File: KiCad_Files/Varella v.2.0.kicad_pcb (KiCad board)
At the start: 4 copper layers, 86 x 86 mm, 97 parts, among them IC1 MAX6682MUA+T, IC2 MAX6682MUA+T, IC3 MAX6682MUA+T, IC4 MMC5983MA, IC5 ZMOD4410AI3V, J1 ESQ-120-39-G-D, J2 Conn_01x12_Male, J3 MEM2075-00-140-01-A, J4 53261-7002, J5 53261-7002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

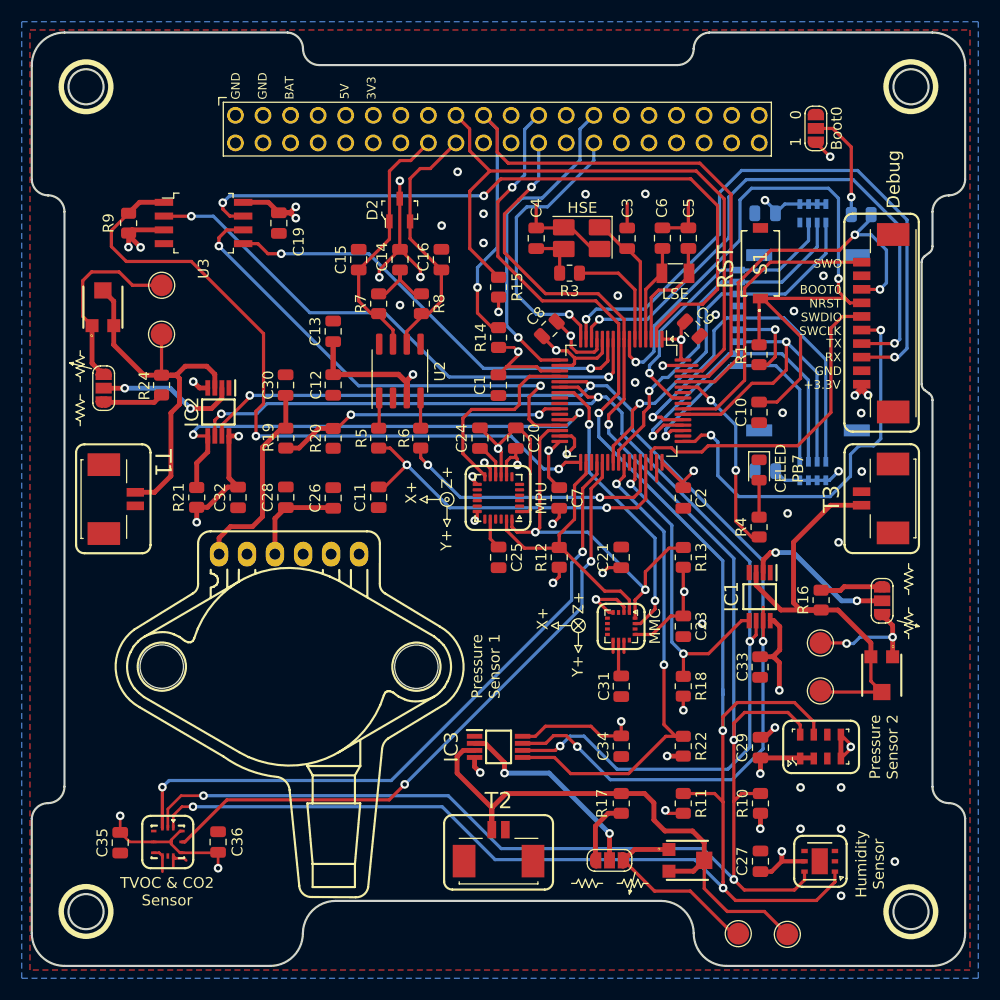
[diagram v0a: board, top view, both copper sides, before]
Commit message: Add Traces to Stack Connector
Connects the Interrupts and PWM pins that come from the EPS boards through the Stack Connector to Varella's STM32.
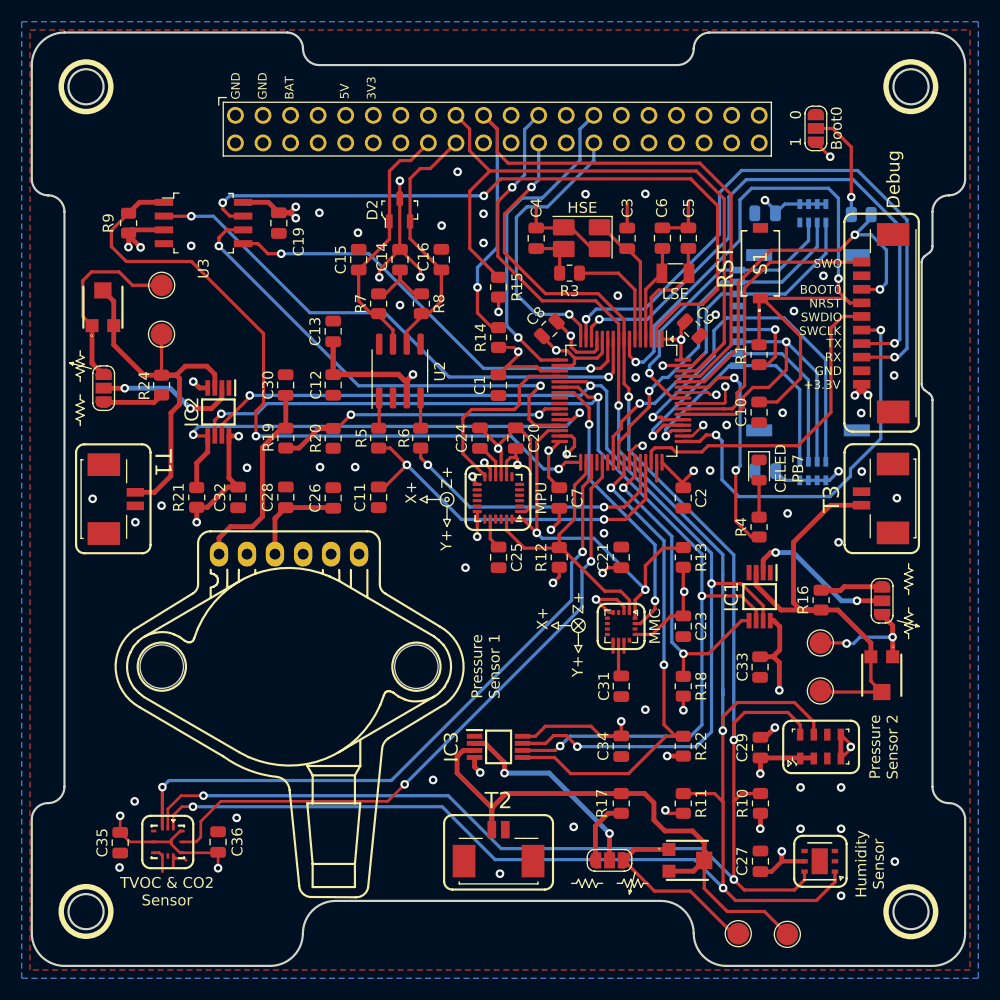
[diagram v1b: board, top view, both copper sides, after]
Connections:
- J1 pad 33: Net-(J1-Pad33) -> EPS_ALRT1
- J1 pad 34: Net-(J1-Pad34) -> EPS_CHRG
- J1 pad 35: Net-(J1-Pad35) -> EPS_THERM_PWM
- J1 pad 37: Net-(J1-Pad37) -> EPS_FAULT
- U1 pad 35: Net-(U1-Pad35) -> ZMOD_INT
- U1 pad 36: ZMOD_INT -> Net-(U1-Pad36)
- U1 pad 42: Net-(U1-Pad42) -> EPS_ALRT1
- U1 pad 50: Net-(U1-Pad50) -> EPS_FAULT
- U1 pad 56: Net-(U1-Pad56) -> EPS_THERM_PWM
- U1 pad 58: Net-(U1-Pad58) -> EPS_CHRG
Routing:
- net EPS_ALRT1: track 0.00 -> 40.2 mm, vias 0 -> 1
- net EPS_FAULT: track 0.00 -> 33.0 mm, vias 0 -> 1
- net EPS_THERM_PWM: track 0.00 -> 31.9 mm, vias 0 -> 1
- net EPS_CHRG: track 0.00 -> 28.8 mm, vias 0 -> 1
- net MAX_SPI_CLK: track 108.9 -> 102.3 mm
- net MAX_SPI_MISO: track 105.8 -> 99.7 mm
- net DEBUG_LED: track 17.9 -> 21.4 mm
- net GND: track 79.9 -> 82.8 mm, vias 37 -> 58
- net SDA_A: track 170.0 -> 168.5 mm
- net SCL_A: track 159.8 -> 158.6 mm
- net CAN_TX: track 34.1 -> 34.9 mm
- net SWO: track 27.1 -> 27.9 mm
- net ZMOD_RST: track 59.9 -> 60.8 mm
- net CAN_RX: track 25.5 -> 26.3 mm
- net BOOT0: track 37.1 -> 36.5 mm
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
